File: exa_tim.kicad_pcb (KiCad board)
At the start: 4 copper layers, 42 x 42 mm, 54 parts, among them J1 Conn_ARM_JTAG_SWD_10, J2 FH12A-24S-0.5SH(55), Q1 SI2333DS-T1-E3, Q2 DMN3067LW-7, SW1 SKHLLFA010, SW2 SKHLLFA010, SW3 SKHLLFA010, SW4 SKHLLFA010, U1 STM32L071KZUx, U2 CAM-M8Q-0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

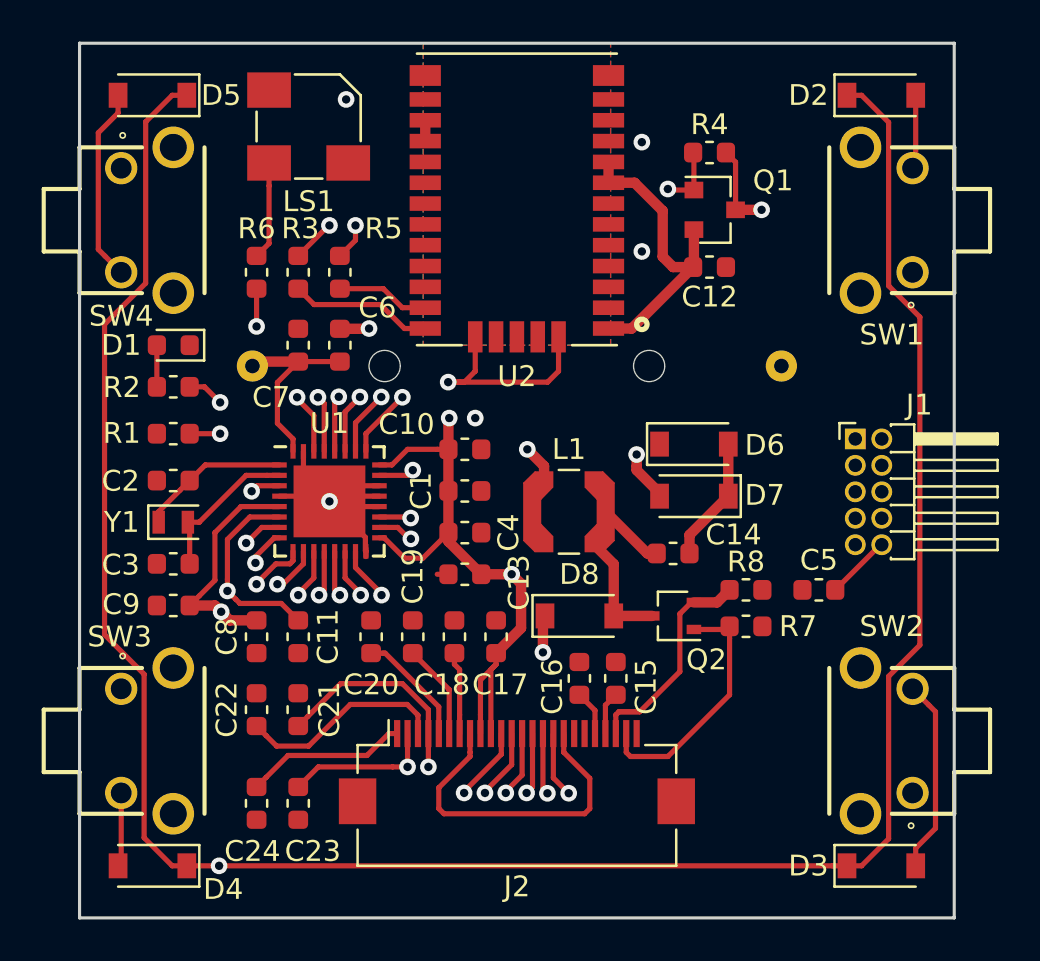
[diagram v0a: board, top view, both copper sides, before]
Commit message: Add name, version and fab instructions to PCB
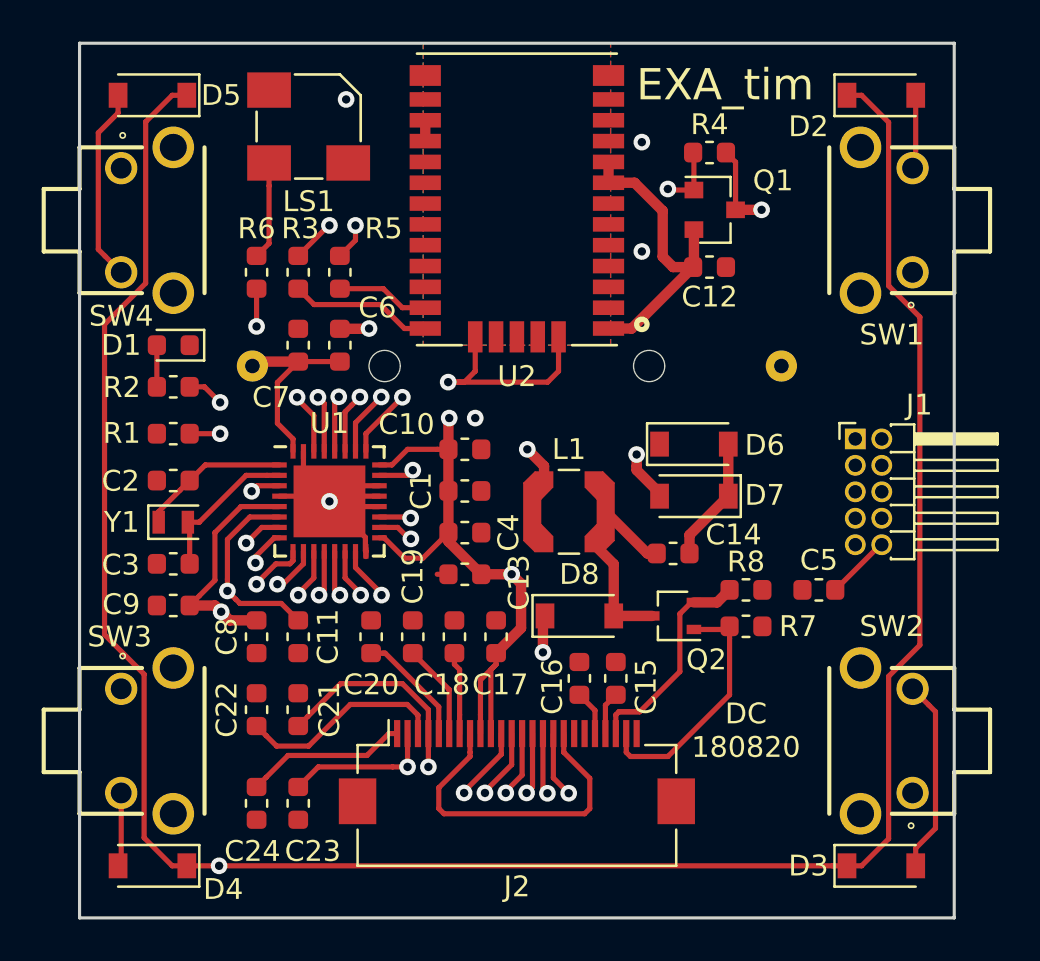
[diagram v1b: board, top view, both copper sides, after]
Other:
- board text added: "DC 180820"
- board text added: "DO NOT FILL THIS AREA WITH COPPER"
- board text added: "EXA_tim"
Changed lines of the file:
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@@
   (general
     (thickness 1.6)
-    (drawings 6)
+    (drawings 9)
     (tracks 496)
     (zones 0)
@@
     (visible_elements 7FFFFFFF)
     (pcbplotparams
-      (layerselection 0x010fc_ffffffff)
+      (layerselection 0x010f0_ffffffff)
       (usegerberextensions false)
-      (usegerberattributes false)
+      (usegerberattributes true)
       (usegerberadvancedattributes false)
       (creategerberjobfile false)
@@
       (outputformat 1)
       (mirror false)
-      (drillshape 1)
+      (drillshape 0)
       (scaleselection 1)
-      (outputdirectory ""))
+      (outputdirectory "gerber/"))
   )
   (net 0 "")
@@
     (tags SOD-123)
     (attr smd)
-    (fp_text reference D2 (at -3.5 0) (layer F.SilkS)
+    (fp_text reference D2 (at -3.5 1.5) (layer F.SilkS)
       (effects (font (size 1 1) (thickness 0.15)))
     )
@@
     )
   )
+  (gr_text "DO NOT\nFILL THIS\nAREA\nWITH\nCOPPER" (at 121 75) (layer F.Fab)
+    (effects (font (size 1 1) (thickness 0.15)))
+  )
+  (gr_text "DC\n180820" (at 132 103) (layer F.SilkS)
+    (effects (font (size 1 1) (thickness 0.15)))
+  )
+  (gr_text EXA_tim (at 131 72) (layer F.SilkS)
+    (effects (font (size 1.5 1.5) (thickness 0.3)))
+  )
   (dimension 42 (width 0.3) (layer Eco1.User)

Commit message: General cleanup
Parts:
- C5: footprint Resistor_SMD:R_0603_1608Metric -> Capacitor_SMD:C_0603_1608Metric
- D1: value LED_ALT -> LTST-C194KSKT
- LS1: value Speaker -> CUI_CSS-0575A-SMT
- R1, R4, R7: value 1M -> 100k
- R8: value 3R -> 3
- U1: footprint Package_DFN_QFN:QFN-32-1EP_5x5mm_P0.5mm_EP3.45x3.45mm -> exa_tim:QFN-32-1EP_5x5mm_P0.5mm_EP3.45x3.45mm

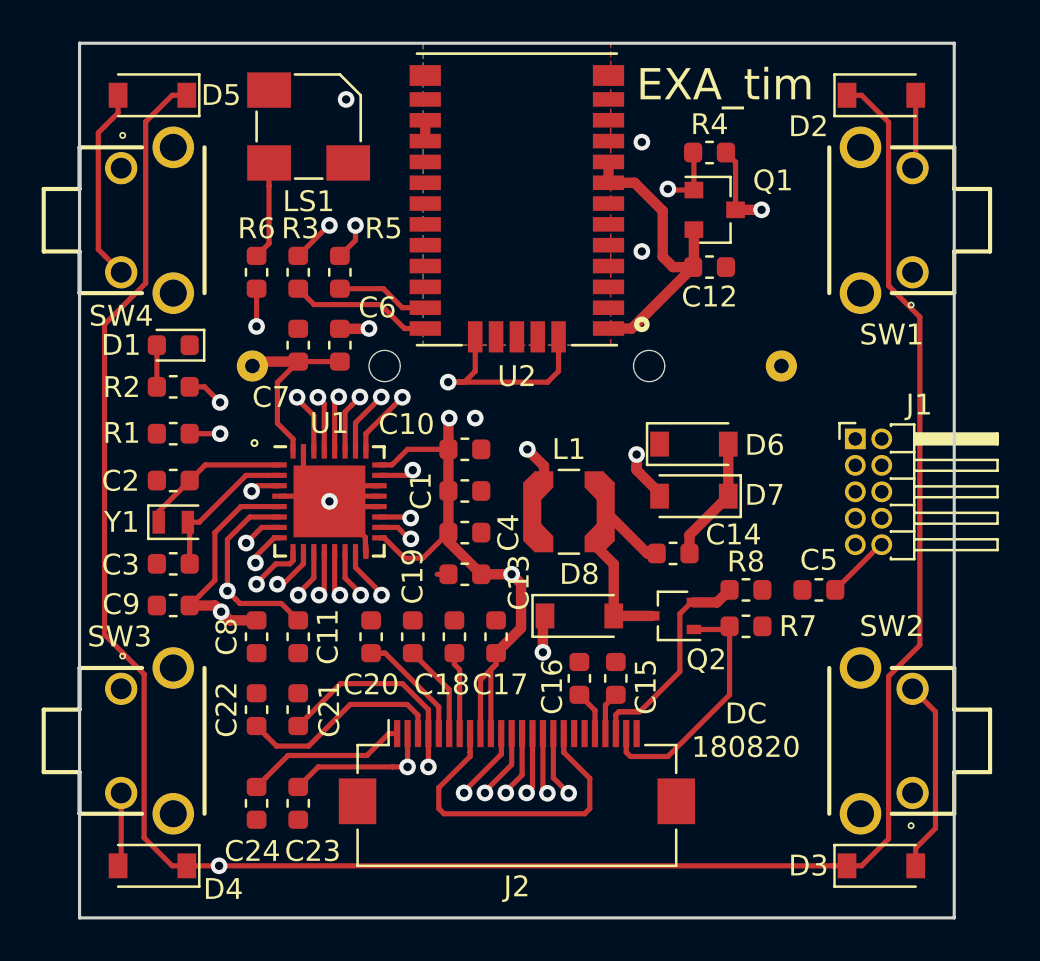
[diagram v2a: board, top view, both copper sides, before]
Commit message: Rework GND plane, power distrubution and PU
PU are now 1M ohm. GND is the only power plane.
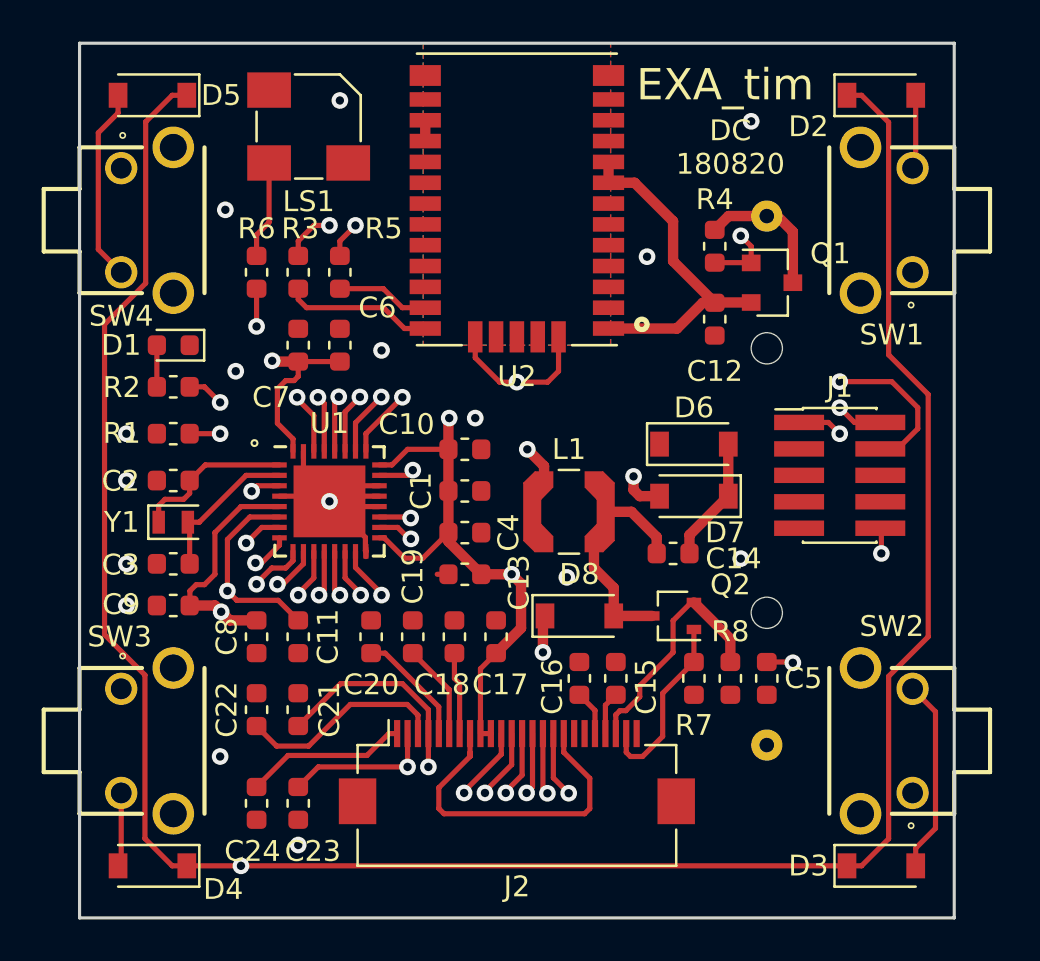
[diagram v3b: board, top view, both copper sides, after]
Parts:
- J1: footprint Connector_PinHeader_1.27mm:PinHeader_2x05_P1.27mm_Horizontal -> Connector_PinHeader_1.27mm:PinHeader_2x05_P1.27mm_Vertical_SMD
- R1, R4, R7: value 100k -> 1M
- moved C5 4.93 mm to (133.0, 100.5), turned to 90 degrees
- moved BT1 4.61 mm to (124.5, 91.0), turned to 90 degrees
- moved R4 4.51 mm to (130.5, 79.8), turned to 270 degrees
- moved Q1 4.45 mm to (133.2, 81.5)
- moved R8 4.32 mm to (131.2, 100.5), turned to 270 degrees
- moved R7 3.54 mm to (129.5, 100.5), turned to 270 degrees
- moved C12 2.51 mm to (130.5, 83.2), turned to 90 degrees
- moved J1 1.90 mm to (136.5, 90.8)
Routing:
- net 3V: track 61.3 -> 231.0 mm, vias 5 -> 6
- net GND: track 79.6 -> 41.6 mm, vias 6 -> 16
- net /NRST: track 61.2 -> 52.8 mm, vias 1 -> 3
- net /GNSS_EN: track 33.6 -> 39.8 mm
- net /BTN1: track 40.1 -> 36.8 mm
- net /GDR: track 12.2 -> 8.98 mm
- net /SWCLK: track 29.8 -> 32.1 mm, vias 1 -> 2
- net /GNSS_VDD: track 15.4 -> 17.0 mm
- net /PREVGL: track 29.3 -> 27.7 mm
- net Net-(C2-Pad1): track 7.24 -> 8.28 mm
- net /RX: track 29.8 -> 29.0 mm
- net /SWDIO: track 26.5 -> 25.7 mm, vias 2 -> 3
- net /CS: track 22.6 -> 23.2 mm
- net /MOSI: track 19.3 -> 19.9 mm
- net /LED: track 14.7 -> 15.3 mm
- added copper zone on B.Cu, net GND
- removed copper zone on B.Cu, net 3V

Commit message: Added 3d models and moved some parts for fitting
The 3d models are not licenced under the permissive licensce.
They come from their manufacturer and some other free sources.
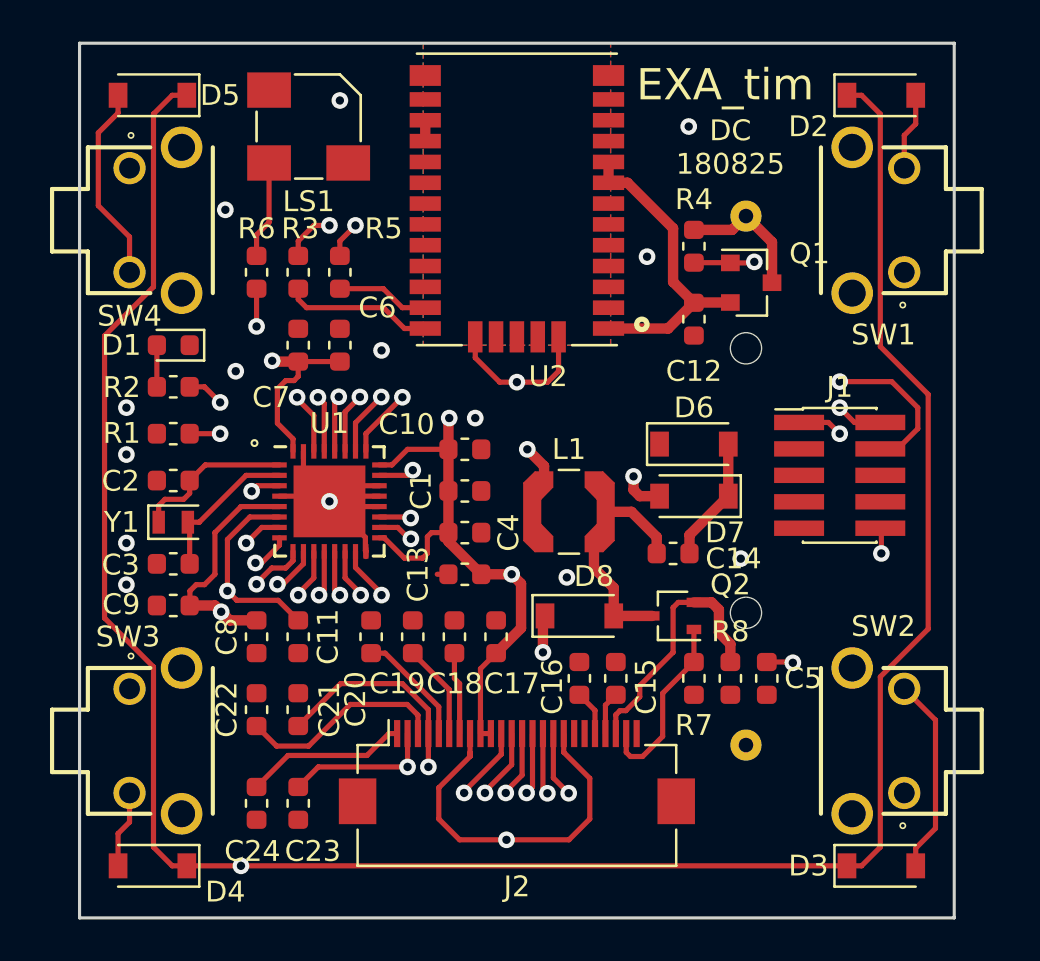
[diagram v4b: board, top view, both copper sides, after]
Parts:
- J2: footprint Connector_FFC-FPC:Hirose_FH12-24S-0.5SH_1x24-1MP_P0.50mm_Horizontal -> exa_tim:Hirose_FH12-24S-0.5SH_1x24-1MP_P0.50mm_Horizontal
- L1: footprint Inductor_SMD:L_Coilcraft_LPS4018 -> exa_tim:L_Coilcraft_LPS4018
- U2: value CAM-M8Q-0 -> CAM-M8C-0
- moved BT1 1.00 mm to (123.5, 91.0)
- moved C12 1.00 mm to (129.5, 83.2)
- moved Q1 1.00 mm to (132.2, 81.5)
- moved R4 1.00 mm to (129.5, 79.8)
- moved SW1 0.40 mm to (141.6, 78.5)
- moved SW2 0.40 mm to (141.6, 103.5)
- moved SW3 0.40 mm to (100.4, 103.5)
- moved SW4 0.40 mm to (100.4, 78.5)
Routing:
- net 3V: track 231.0 -> 212.2 mm
- net GND: track 41.6 -> 43.3 mm, vias 16 -> 15
- net /GNSS_VDD: track 17.0 -> 15.4 mm
- net /GNSS_EN: track 39.8 -> 38.4 mm
- net /RESE: track 11.7 -> 12.5 mm
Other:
- board text added: "DC 180825"
- board text removed: "DC 180820"
